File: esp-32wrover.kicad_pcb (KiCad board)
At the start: 2 copper layers, 68.6 x 53.3 mm, 90 parts, among them CON1 BARREL_JACK, P1 Power, P2 Analog, P3 Digital, P4 Digital, P5 CONN_1, P6 CONN_1, P7 CONN_1, P8 CONN_1, P9 CONN_01X04, Q1 12Mhz, Q2 32.768Khz, Q3 Q_NPN_BEC, Q4 Q_NPN_BEC, SW1 SW_PUSH, SW2 SW_PUSH, U1 usb_mini_b, U2 MCP16311-MNY, U3 BD00GA5WEFJ, U4 PL2303HXA, U5 MCP6001R, U6 ESP32-WROVER, U7 IRLM6402

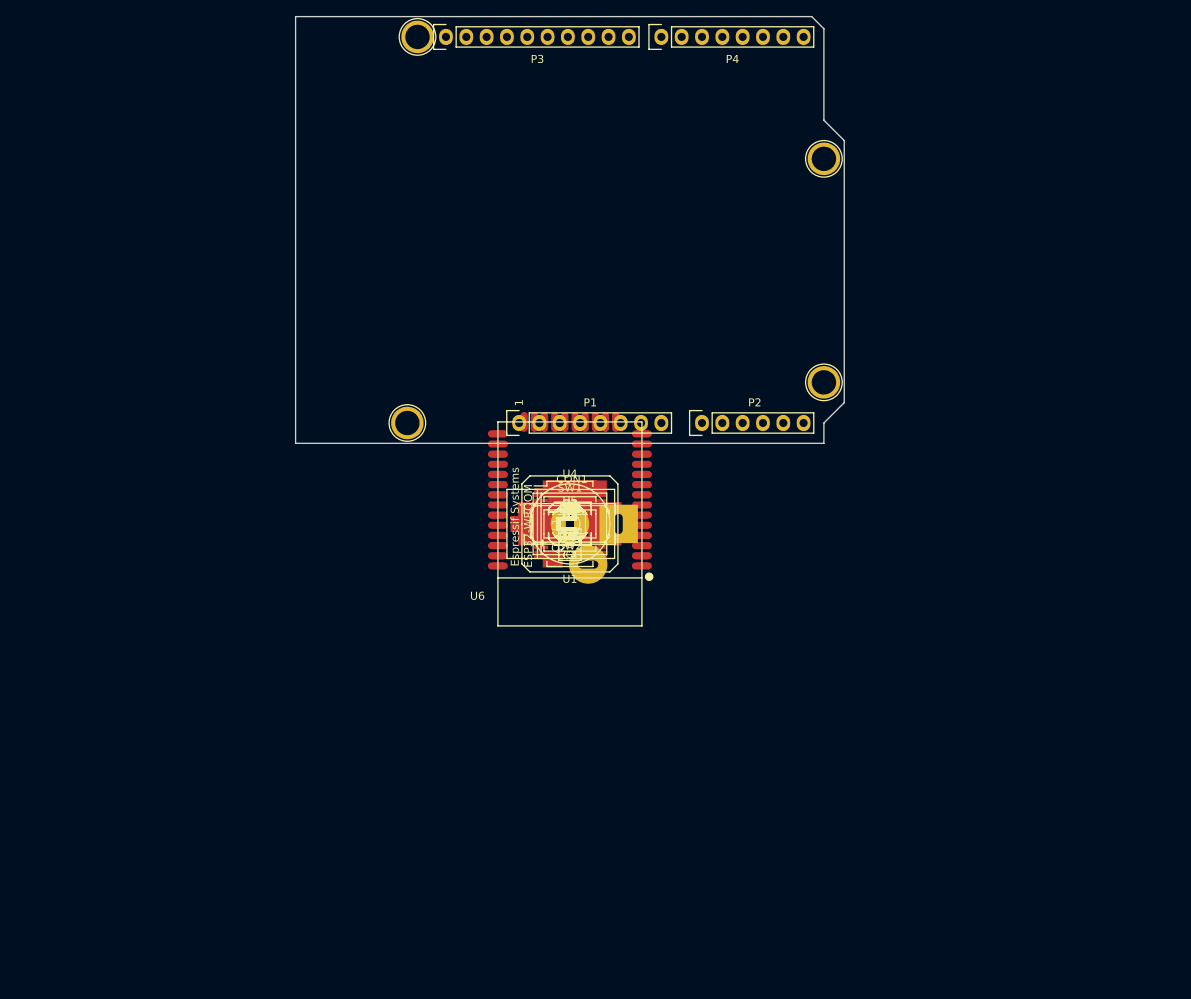
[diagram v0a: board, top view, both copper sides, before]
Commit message: thêm header ICSP
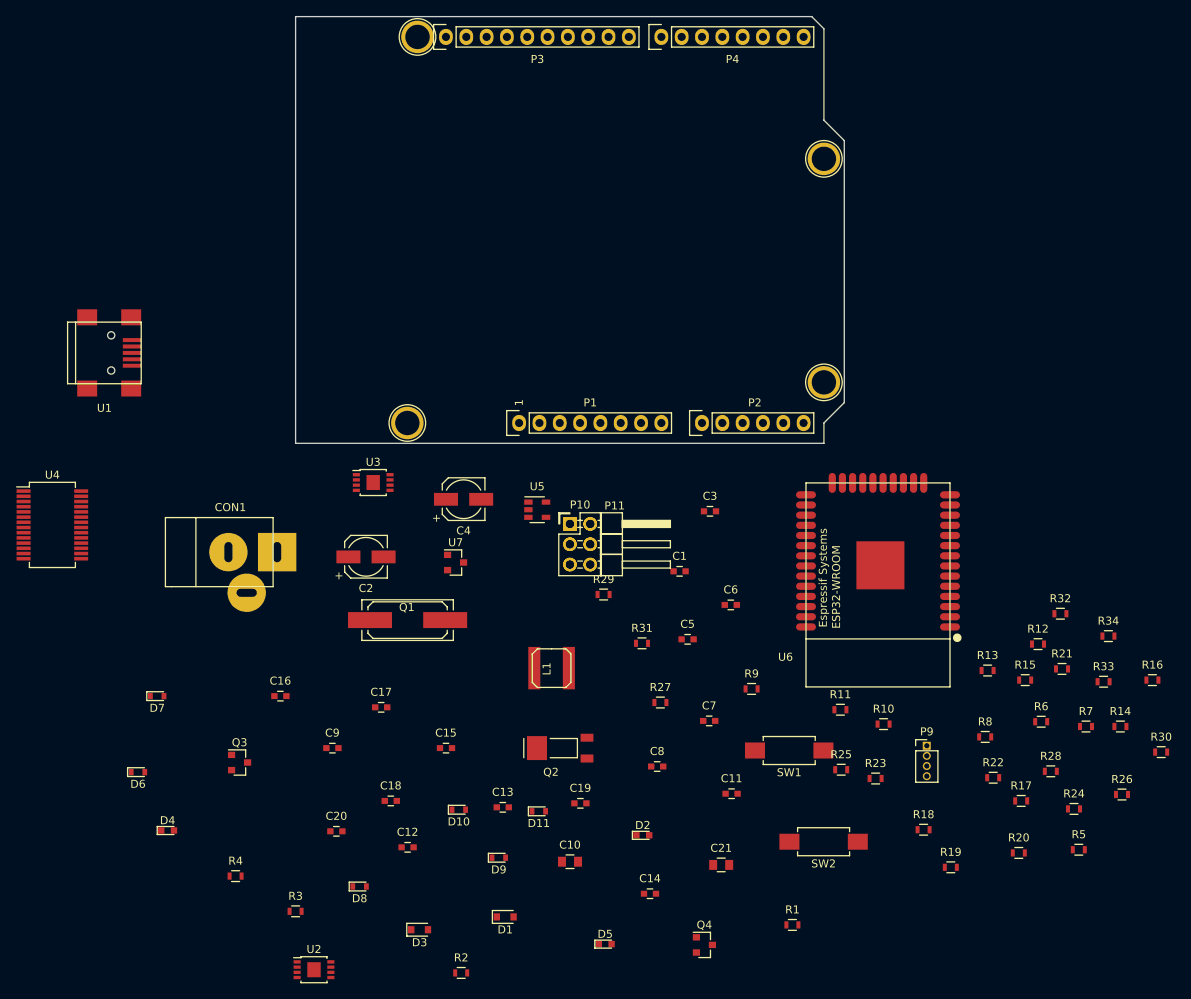
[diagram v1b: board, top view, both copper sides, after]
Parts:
- added P10: ICSP, Pin_Headers:Pin_Header_Straight_2x03_Pitch2.54mm, F.Cu at (145.3, 136.4)
- added P11: ICSP-1, Pin_Headers:Pin_Header_Angled_2x03_Pitch2.54mm, F.Cu at (145.3, 136.4)
- L1: footprint Inductors:SELF-WE-PD-XXL -> Inductors:SELF-WE-TPC_M
- SW1: footprint Buttons_Switches_SMD:SW_SPST_B3SL-1022P -> Buttons_Switches_SMD:SW_SPST_REED_CT05-XXXX-G1
- moved R30 79.2 mm to (219.2, 165.0)
- moved R26 76.9 mm to (214.3, 170.3)
- moved R5 75.5 mm to (208.9, 177.2)
- moved R16 75.4 mm to (218.1, 156.0)
- moved R14 73.3 mm to (214.1, 161.8)
- moved R24 72.4 mm to (208.3, 172.1)
- moved R20 69.6 mm to (201.4, 177.6)
- moved R33 69.6 mm to (212.0, 156.2)
- moved R7 69.3 mm to (209.8, 161.8)
- moved R34 68.8 mm to (212.6, 150.5)
- moved R28 67.6 mm to (205.4, 167.4)
- moved R17 66.2 mm to (201.7, 171.1)
- moved U4 64.7 mm to (80.6, 136.6)
- moved U2 64.3 mm to (113.3, 192.2)
- moved R21 64.1 mm to (206.8, 154.6)
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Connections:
- net /IOREF renamed Net-(P1-Pad2)
- C19 pad 2: +5V -> VCC
- C5 pad 2: +5V -> VCC
- D10 pad 2: Net-(D10-Pad2) -> A5
- D11 pad 2: Net-(D11-Pad2) -> A3
- D3 pad 1: +5V -> VCC
- D7 pad 2: Net-(D7-Pad2) -> A1
- D8 pad 2: Net-(D8-Pad2) -> A2
- D9 pad 2: Net-(D9-Pad2) -> A4
- P1 pad 1: Net-(P1-Pad1) -> IO18
- P2 pad 4: A4 -> A3
- P2 pad 5: A5 -> A4
- P2 pad 6: A6 -> A5
- U1 pad 1: +5V -> VCC
- U4 pad 20: +5V -> VCC
- U6 pad 10: ADC-4 -> A4
- U6 pad 11: ADC-5 -> A5
- U6 pad 5: ADC-1 -> A1
- U6 pad 6: ADC-2 -> A2
- U6 pad 7: ADC-3 -> A3
- U7 pad 2: Net-(U7-Pad2) -> VCC
- U7 pad 3: Net-(U7-Pad3) -> +5V
